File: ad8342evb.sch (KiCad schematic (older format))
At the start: 96 parts, among them J1 PWR_in_direct, J10 Bat, J11 3V3, J12 PWR_Jumper, J13 TP1, J14 TP1, J15 TP_PWR, J16 TP2, J17 TP3, J2 RF_in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

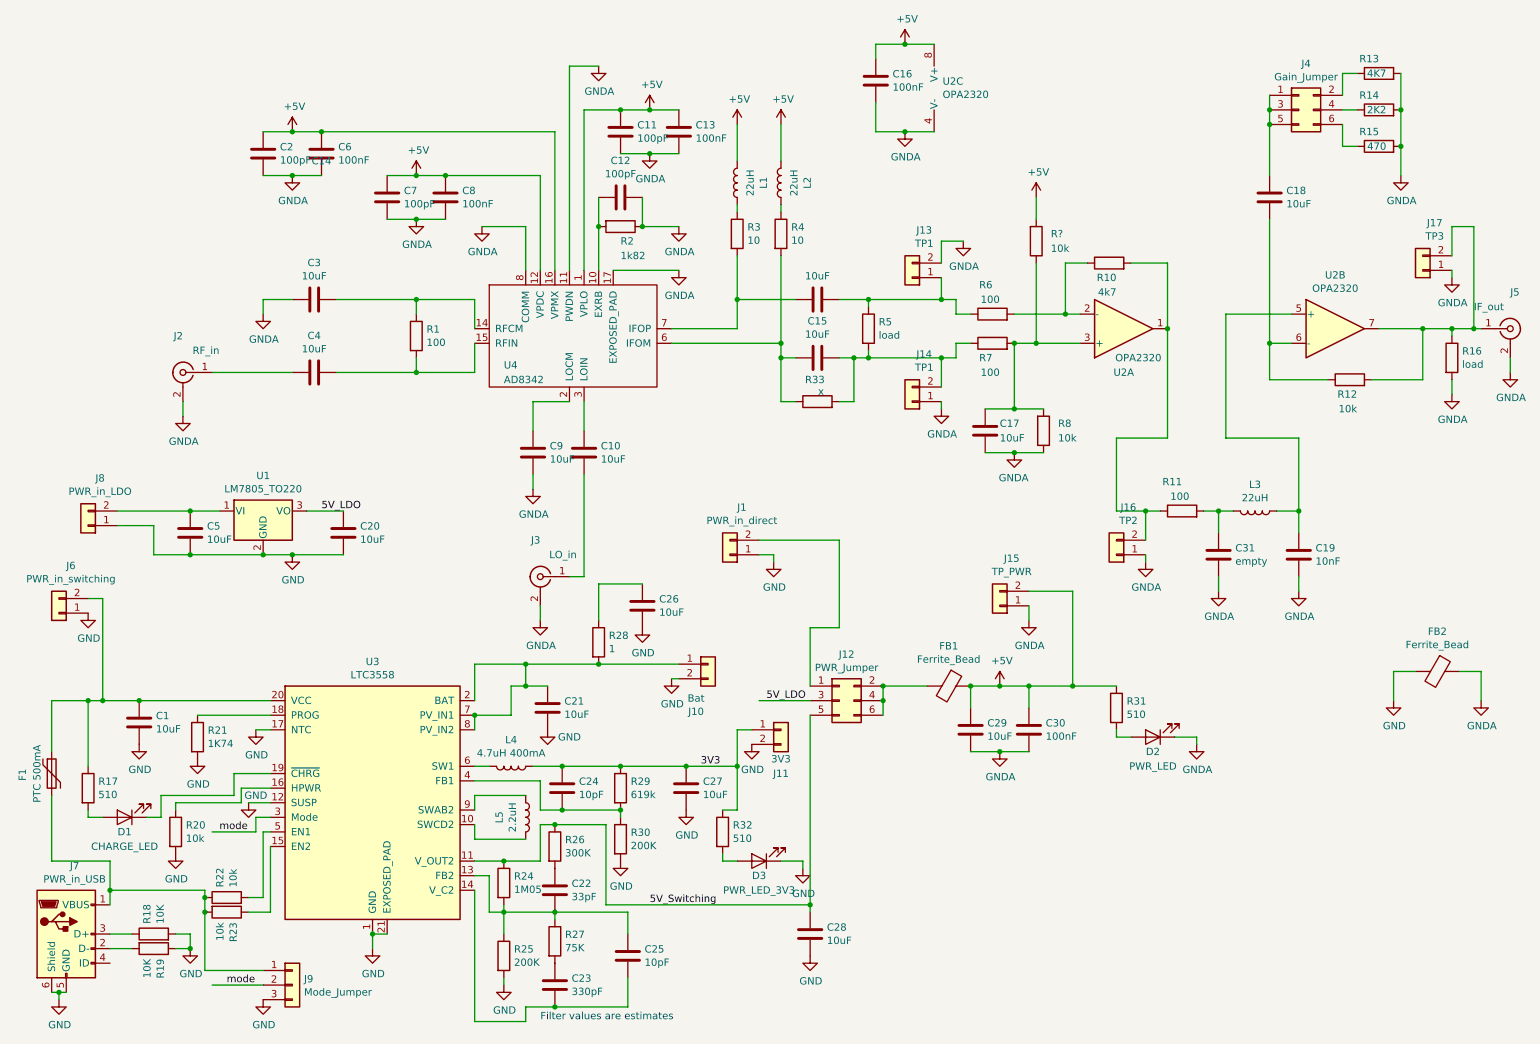
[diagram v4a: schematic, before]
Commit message: update component values
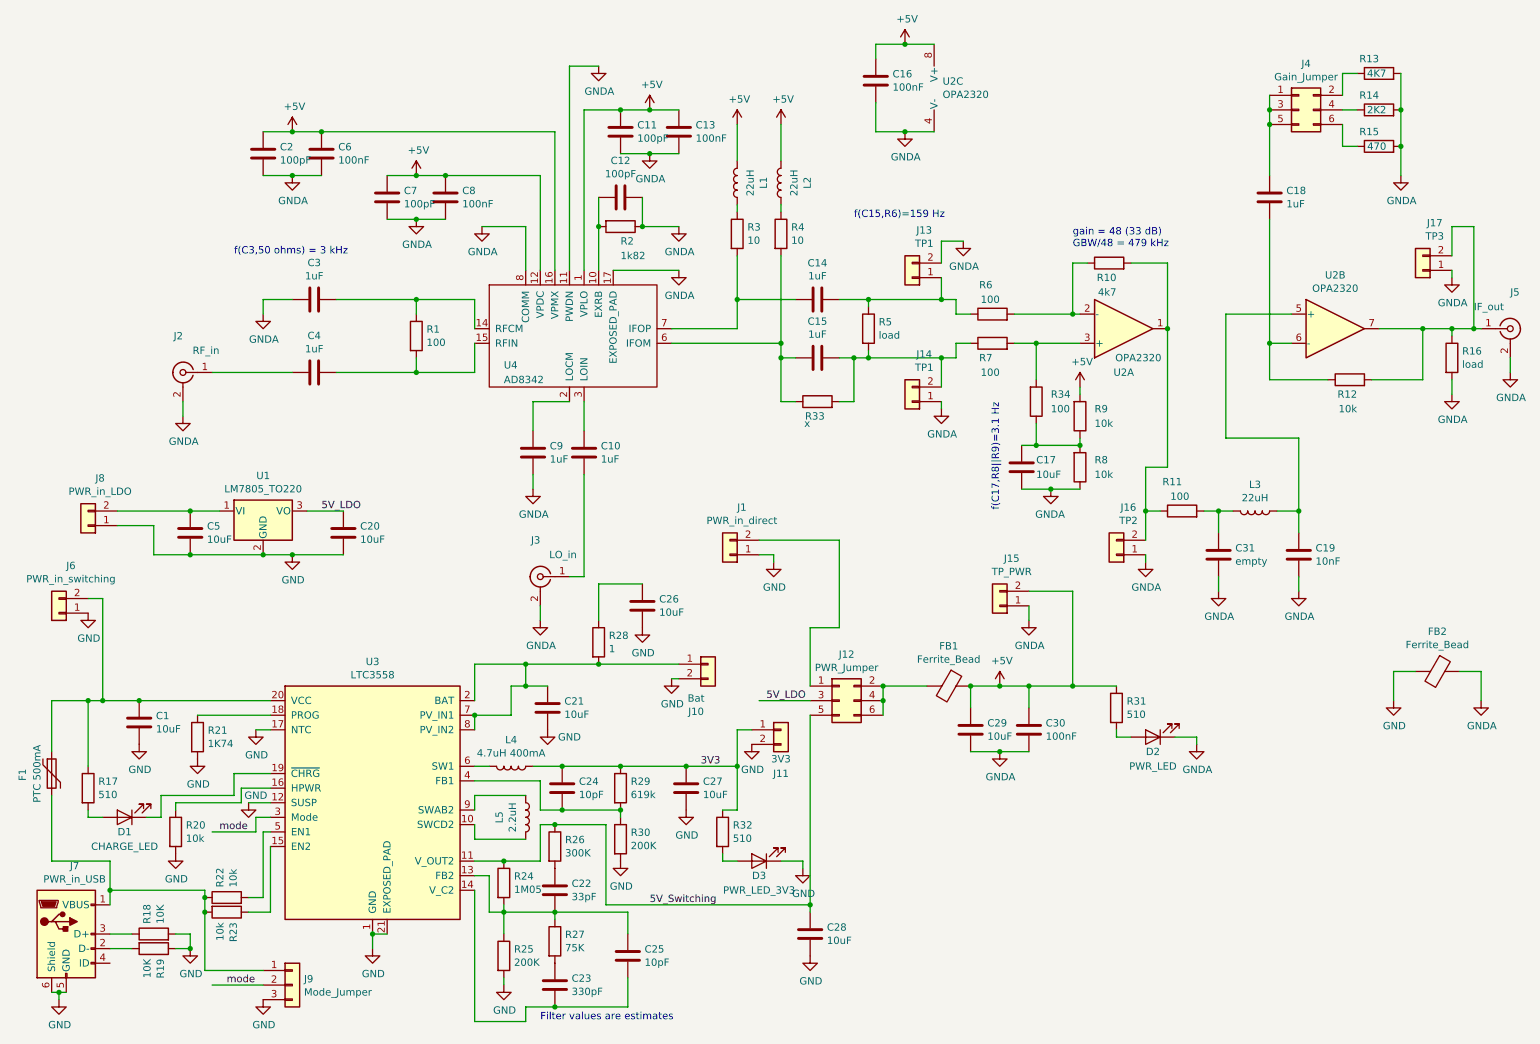
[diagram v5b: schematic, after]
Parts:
- added R34: 100, Resistor_SMD:R_0805_2012Metric_Pad1.15x1.40mm_HandSolder, symbol Device:R
- C10, C14, C15, C18, C3, C4, C9: value 10uF -> 1uF
- gave numbers to parts that had none: 1
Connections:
- net at C17.2, R8.2, R9.1: now also R34.1; no longer R7.2, U2.3 (+)
- new net: R34.2, R7.2, U2.3 (+)
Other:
- note added: "f(C15,R6)=159 Hz"
- note added: "f(C17,R8||R9)=3.1 Hz"
- note added: "f(C3,50 ohms) = 3 kHz"
- note added: "gain = 48 (33 dB)\nGBW/48 = 479 kHz"
- moved on the sheet: C17, R8, R9
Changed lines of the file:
@@
 P 2550 3300
 F 0 "C4" V 2298 3300 50  0000 C CNN
-F 1 "10uF" V 2389 3300 50  0000 C CNN
+F 1 "1uF" V 2389 3300 50  0000 C CNN
 F 2 "Capacitor_SMD:C_0805_2012Metric_Pad1.15x1.40mm_HandSolder" H 2588 3150 50  0001 C CNN
 F 3 "~" H 2550 3300 50  0001 C CNN
@@
 P 2550 2800
 F 0 "C3" V 2298 2800 50  0000 C CNN
-F 1 "10uF" V 2389 2800 50  0000 C CNN
+F 1 "1uF" V 2389 2800 50  0000 C CNN
 F 2 "Capacitor_SMD:C_0805_2012Metric_Pad1.15x1.40mm_HandSolder" H 2588 2650 50  0001 C CNN
 F 3 "~" H 2550 2800 50  0001 C CNN
@@
 P 4050 3850
 F 0 "C9" H 4165 3896 50  0000 L CNN
-F 1 "10uF" H 4165 3805 50  0000 L CNN
+F 1 "1uF" H 4165 3805 50  0000 L CNN
 F 2 "Capacitor_SMD:C_0805_2012Metric_Pad1.15x1.40mm_HandSolder" H 4088 3700 50  0001 C CNN
 F 3 "~" H 4050 3850 50  0001 C CNN
@@
 P 4400 3850
 F 0 "C10" H 4515 3896 50  0000 L CNN
-F 1 "10uF" H 4515 3805 50  0000 L CNN
+F 1 "1uF" H 4515 3805 50  0000 L CNN
 F 2 "Capacitor_SMD:C_0805_2012Metric_Pad1.15x1.40mm_HandSolder" H 4438 3700 50  0001 C CNN
 F 3 "~" H 4400 3850 50  0001 C CNN
@@
 	4400 4700 4400 4000
 $Comp
-L Device:C C14
-U 1 1 5F199412
-P 6000 2800
-F 0 "C14" V 6950 6200 50  0000 C CNN
-F 1 "10uF" V 6161 2800 50  0000 C CNN
-F 2 "Capacitor_SMD:C_0805_2012Metric_Pad1.15x1.40mm_HandSolder" H 6038 2650 50  0001 C CNN
-F 3 "~" H 6000 2800 50  0001 C CNN
-	1    6000 2800
-	0    -1   -1   0
-$EndComp
-$Comp
 L Device:C C15
 U 1 1 5F1999EF
 P 6000 3200
-F 0 "C15" V 6252 3200 50  0000 C CNN
-F 1 "10uF" V 6161 3200 50  0000 C CNN
+F 0 "C15" V 6250 3200 50  0000 C CNN
+F 1 "1uF" V 6161 3200 50  0000 C CNN
 F 2 "Capacitor_SMD:C_0805_2012Metric_Pad1.15x1.40mm_HandSolder" H 6038 3050 50  0001 C CNN
 F 3 "~" H 6000 3200 50  0001 C CNN
@@
 L Device:R R8
 U 1 1 5F200A58
-P 7550 3700
-F 0 "R8" H 7650 3650 50  0000 L CNN
-F 1 "10k" H 7650 3750 50  0000 L CNN
-F 2 "Resistor_SMD:R_0805_2012Metric_Pad1.15x1.40mm_HandSolder" V 7480 3700 50  0001 C CNN
-F 3 "~" H 7550 3700 50  0001 C CNN
-	1    7550 3700
+P 7800 3950
+F 0 "R8" H 7900 3900 50  0000 L CNN
+F 1 "10k" H 7900 4000 50  0000 L CNN
+F 2 "Resistor_SMD:R_0805_2012Metric_Pad1.15x1.40mm_HandSolder" V 7730 3950 50  0001 C CNN
+F 3 "~" H 7800 3950 50  0001 C CNN
+	1    7800 3950
 	1    0    0    1
 $EndComp
@@
 	9300 4250 9300 4400
 Wire Wire Line
-	8400 3750 8050 3750
-Wire Wire Line
-	8050 3750 8050 4250
-Wire Wire Line
 	9300 4250 9300 3750
 Wire Wire Line
@@
 P 9100 2100
 F 0 "C18" H 9215 2146 50  0000 L CNN
-F 1 "10uF" H 9215 2055 50  0000 L CNN
+F 1 "1uF" H 9215 2055 50  0000 L CNN
 F 2 "Capacitor_SMD:C_0805_2012Metric_Pad1.15x1.40mm_HandSolder" H 9138 1950 50  0001 C CNN
 F 3 "~" H 9100 2100 50  0001 C CNN
@@
 L Device:C C17
 U 1 1 5F280D97
-P 7150 3700
-F 0 "C17" H 7250 3650 50  0000 L CNN
-F 1 "10uF" H 7250 3750 50  0000 L CNN
-F 2 "Capacitor_SMD:C_0805_2012Metric_Pad1.15x1.40mm_HandSolder" H 7188 3550 50  0001 C CNN
-F 3 "~" H 7150 3700 50  0001 C CNN
-	1    7150 3700
+P 7400 3950
+F 0 "C17" H 7500 3900 50  0000 L CNN
+F 1 "10uF" H 7500 4000 50  0000 L CNN
+F 2 "Capacitor_SMD:C_0805_2012Metric_Pad1.15x1.40mm_HandSolder" H 7438 3800 50  0001 C CNN
+F 3 "~" H 7400 3950 50  0001 C CNN
+	1    7400 3950
 	1    0    0    1
 $EndComp
@@
 Connection ~ 6450 5450
 Wire Wire Line
-	8050 4250 8250 4250
-Connection ~ 8250 4250
-Wire Wire Line
 	8250 4250 8350 4250
 $Comp
@@
 L power:GNDA #PWR0111
 U 1 1 5F336EFE
-P 7350 3850
-F 0 "#PWR0111" H 7350 3600 50  0001 C CNN
-F 1 "GNDA" H 7355 3677 50  0000 C CNN
-F 2 "" H 7350 3850 50  0001 C CNN
-F 3 "" H 7350 3850 50  0001 C CNN
-	1    7350 3850
+P 7600 4100
+F 0 "#PWR0111" H 7600 3850 50  0001 C CNN
+F 1 "GNDA" H 7605 3927 50  0000 C CNN
+F 2 "" H 7600 4100 50  0001 C CNN
+F 3 "" H 7600 4100 50  0001 C CNN
+	1    7600 4100
 	-1   0    0    -1
 $EndComp
@@
 U 1 1 5F30BE35
 P 6000 3500
-F 0 "R33" V 6150 3450 50  0000 L CNN
-F 1 "x" V 6070 3455 50  0000 L CNN
+F 0 "R33" V 5900 3450 50  0000 L CNN
+F 1 "x" V 5850 3550 50  0000 L CNN
 F 2 "Resistor_SMD:R_0805_2012Metric_Pad1.15x1.40mm_HandSolder" V 5930 3500 50  0001 C CNN
 F 3 "~" H 6000 3500 50  0001 C CNN
@@
 Wire Wire Line
 	6250 3200 6150 3200
-Connection ~ 7350 3100
-Wire Wire Line
-	7350 3100 7500 3100
 Wire Wire Line
 	8150 2550 8400 2550
@@
 	8400 2550 8400 3000
 Connection ~ 8400 3000
-Wire Wire Line
-	8400 3000 8400 3750
-$Comp
-L Device:R R?
+$Comp
+L Device:R R9
 U 1 1 5F4F3D38
-P 7500 2400
-F 0 "R?" H 7600 2350 50  0000 L CNN
-F 1 "10k" H 7600 2450 50  0000 L CNN
-F 2 "Resistor_SMD:R_0805_2012Metric_Pad1.15x1.40mm_HandSolder" V 7430 2400 50  0001 C CNN
-F 3 "~" H 7500 2400 50  0001 C CNN
-	1    7500 2400
+P 7800 3600
+F 0 "R9" H 7900 3550 50  0000 L CNN
+F 1 "10k" H 7900 3650 50  0000 L CNN
+F 2 "Resistor_SMD:R_0805_2012Metric_Pad1.15x1.40mm_HandSolder" V 7730 3600 50  0001 C CNN
+F 3 "~" H 7800 3600 50  0001 C CNN
+	1    7800 3600
 	1    0    0    1
 $EndComp
-Wire Wire Line
-	7350 2900 7700 2900
-Wire Wire Line
-	7700 2900 7700 2550
-Wire Wire Line
-	7700 2550 7850 2550
-Connection ~ 7700 2900
-Wire Wire Line
-	7700 2900 7800 2900
-Wire Wire Line
-	7500 2550 7500 3100
+$Comp
+L power:+5V #PWR0155
+U 1 1 5F5852E9
+P 7800 3400
+F 0 "#PWR0155" H 7800 3250 50  0001 C CNN
+F 1 "+5V" H 7815 3573 50  0000 C CNN
+F 2 "" H 7800 3400 50  0001 C CNN
+F 3 "" H 7800 3400 50  0001 C CNN
+	1    7800 3400
+	1    0    0    -1
+$EndComp
+Wire Wire Line
+	7400 4100 7600 4100
+Connection ~ 7600 4100
+Wire Wire Line
+	7600 4100 7800 4100
+Wire Wire Line
+	7400 3800 7500 3800
+Wire Wire Line
+	7350 3100 7500 3100
+Wire Wire Line
+	7800 3400 7800 3450
+Wire Wire Line
+	7800 3750 7800 3800
+Connection ~ 7800 3800
+$Comp
+L Device:R R34
+U 1 1 5F782B2E
+P 7500 3500
+F 0 "R34" H 7600 3450 50  0000 L CNN
+F 1 "100" H 7600 3550 50  0000 L CNN
+F 2 "Resistor_SMD:R_0805_2012Metric_Pad1.15x1.40mm_HandSolder" V 7430 3500 50  0001 C CNN
+F 3 "~" H 7500 3500 50  0001 C CNN
+	1    7500 3500
+	1    0    0    1
+$EndComp
+Wire Wire Line
+	7350 2900 7750 2900
+Wire Wire Line
+	7850 2550 7750 2550
+Wire Wire Line
+	7750 2550 7750 2900
+Connection ~ 7750 2900
+Wire Wire Line
+	7750 2900 7800 2900
+Wire Wire Line
+	7500 3350 7500 3100
 Connection ~ 7500 3100
 Wire Wire Line
 	7500 3100 7800 3100
-$Comp
-L power:+5V #PWR?
-U 1 1 5F5852E9
-P 7500 2100
-F 0 "#PWR?" H 7500 1950 50  0001 C CNN
-F 1 "+5V" H 7515 2273 50  0000 C CNN
-F 2 "" H 7500 2100 50  0001 C CNN
-F 3 "" H 7500 2100 50  0001 C CNN
-	1    7500 2100
-	1    0    0    -1
-$EndComp
-Wire Wire Line
-	7500 2100 7500 2250
-Wire Wire Line
-	7150 3550 7350 3550
-Wire Wire Line
-	7150 3850 7350 3850
-Connection ~ 7350 3850
-Wire Wire Line
-	7350 3850 7550 3850
-Wire Wire Line
-	7350 3100 7350 3550
-Connection ~ 7350 3550
-Wire Wire Line
-	7350 3550 7550 3550
+Wire Wire Line
+	7500 3650 7500 3800
+Connection ~ 7500 3800
+Wire Wire Line
+	7500 3800 7800 3800
+Text Notes 7750 2450 0    50   ~ 0
+gain = 48 (33 dB)\nGBW/48 = 479 kHz
+Text Notes 6250 2250 0    50   ~ 0
+f(C15,R6)=159 Hz
+Text Notes 7250 4250 1    50   ~ 0
+f(C17,R8||R9)=3.1 Hz
+Text Notes 2000 2500 0    50   ~ 0
+f(C3,50 ohms) = 3 kHz
+$Comp
+L Device:C C14
+U 1 1 5F8894E7
+P 6000 2800
+F 0 "C14" V 6250 2800 50  0000 C CNN
+F 1 "1uF" V 6161 2800 50  0000 C CNN
+F 2 "Capacitor_SMD:C_0805_2012Metric_Pad1.15x1.40mm_HandSolder" H 6038 2650 50  0001 C CNN
+F 3 "~" H 6000 2800 50  0001 C CNN
+	1    6000 2800
+	0    -1   -1   0
+$EndComp
+Wire Wire Line
+	8400 3950 8250 3950
+Wire Wire Line
+	8250 3950 8250 4250
+Wire Wire Line
+	8400 3000 8400 3950
+Connection ~ 8250 4250
 $EndSCHEMATC

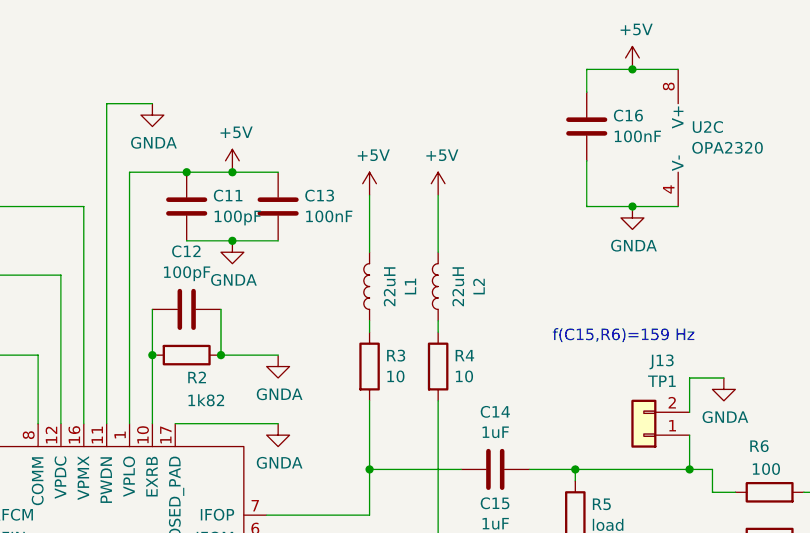
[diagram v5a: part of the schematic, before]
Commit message: added more decoupling caps
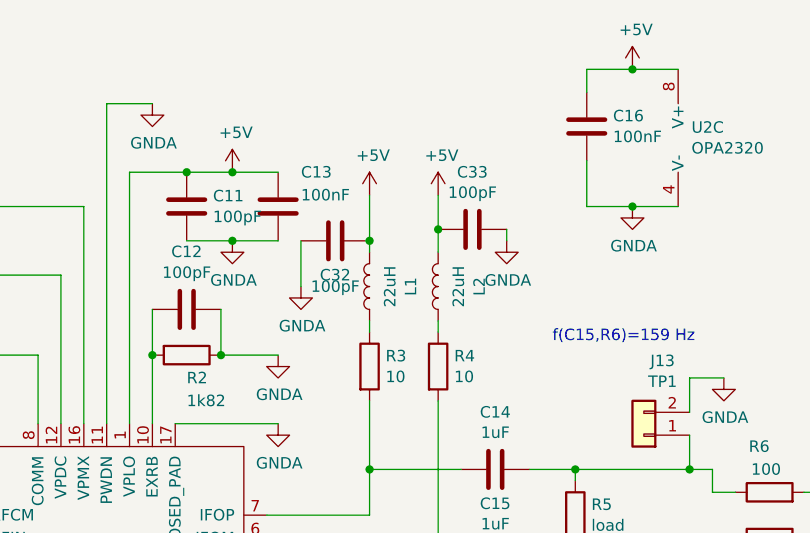
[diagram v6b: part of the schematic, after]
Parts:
- added C32, C33: 100pF, Capacitor_SMD:C_0805_2012Metric_Pad1.15x1.40mm_HandSolder, symbol Device:C
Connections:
- net +5V: now also C32.2, C33.1
- net GNDA: now also C32.1, C33.2
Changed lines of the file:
@@
 U 1 1 5F1ABC3C
 P 5050 1650
-F 0 "C13" H 5165 1696 50  0000 L CNN
-F 1 "100nF" H 5165 1605 50  0000 L CNN
+F 0 "C13" H 5150 1800 50  0000 L CNN
+F 1 "100nF" H 5150 1700 50  0000 L CNN
 F 2 "Capacitor_SMD:C_0805_2012Metric_Pad1.15x1.40mm_HandSolder" H 5088 1500 50  0001 C CNN
 F 3 "~" H 5050 1650 50  0001 C CNN
@@
 	-1   0    0    1
 $EndComp
-Wire Wire Line
-	5750 1850 5750 1600
-Wire Wire Line
-	5450 1850 5450 1600
 $Comp
 L Device:C C31
@@
 	8400 3000 8400 3950
 Connection ~ 8250 4250
+$Comp
+L Device:C C33
+U 1 1 5F2E9B82
+P 5900 1750
+F 0 "C33" V 6150 1750 50  0000 C CNN
+F 1 "100pF" V 6061 1750 50  0000 C CNN
+F 2 "Capacitor_SMD:C_0805_2012Metric_Pad1.15x1.40mm_HandSolder" H 5938 1600 50  0001 C CNN
+F 3 "~" H 5900 1750 50  0001 C CNN
+	1    5900 1750
+	0    -1   -1   0
+$EndComp
+$Comp
+L Device:C C32
+U 1 1 5F301F3A
+P 5300 1800
+F 0 "C32" V 5150 1800 50  0000 C CNN
+F 1 "100pF" V 5100 1800 50  0000 C CNN
+F 2 "Capacitor_SMD:C_0805_2012Metric_Pad1.15x1.40mm_HandSolder" H 5338 1650 50  0001 C CNN
+F 3 "~" H 5300 1800 50  0001 C CNN
+	1    5300 1800
+	0    -1   -1   0
+$EndComp
+Wire Wire Line
+	5450 1600 5450 1800
+Connection ~ 5450 1800
+Wire Wire Line
+	5450 1800 5450 1850
+Wire Wire Line
+	5750 1600 5750 1750
+Connection ~ 5750 1750
+Wire Wire Line
+	5750 1750 5750 1850
+$Comp
+L power:GNDA #PWR0156
+U 1 1 5F34BC62
+P 6050 1800
+F 0 "#PWR0156" H 6050 1550 50  0001 C CNN
+F 1 "GNDA" H 6055 1627 50  0000 C CNN
+F 2 "" H 6050 1800 50  0001 C CNN
+F 3 "" H 6050 1800 50  0001 C CNN
+	1    6050 1800
+	1    0    0    -1
+$EndComp
+$Comp
+L power:GNDA #PWR0157
+U 1 1 5F3641AF
+P 5150 2000
+F 0 "#PWR0157" H 5150 1750 50  0001 C CNN
+F 1 "GNDA" H 5155 1827 50  0000 C CNN
+F 2 "" H 5150 2000 50  0001 C CNN
+F 3 "" H 5150 2000 50  0001 C CNN
+	1    5150 2000
+	1    0    0    -1
+$EndComp
+Wire Wire Line
+	6050 1750 6050 1800
+Wire Wire Line
+	5150 1800 5150 2000
 $EndSCHEMATC
